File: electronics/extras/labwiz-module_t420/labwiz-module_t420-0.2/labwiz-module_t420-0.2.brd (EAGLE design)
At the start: 65.8 x 35.2 mm, 47 parts, among them IC1 MCP3424, U1 MCP9800

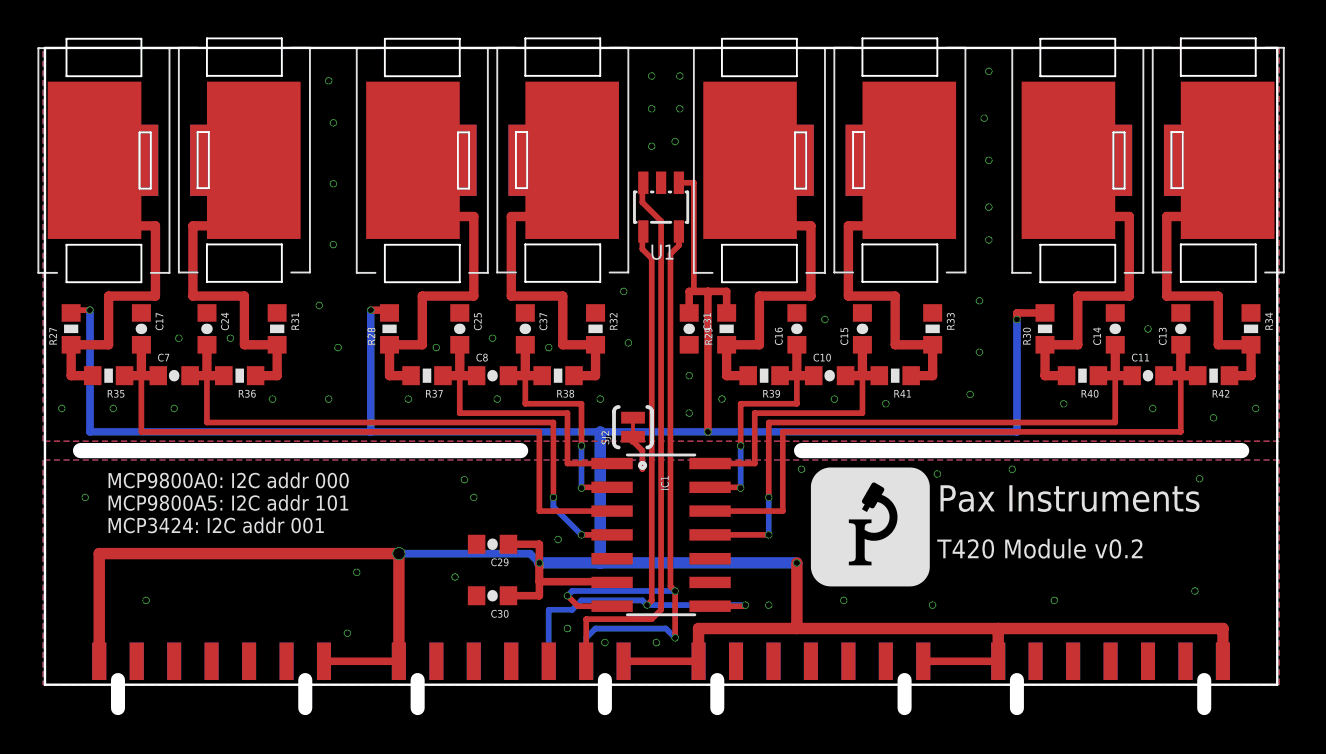
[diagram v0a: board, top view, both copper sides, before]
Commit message: Updated full-breakout and T420 modules. Boards ordered.
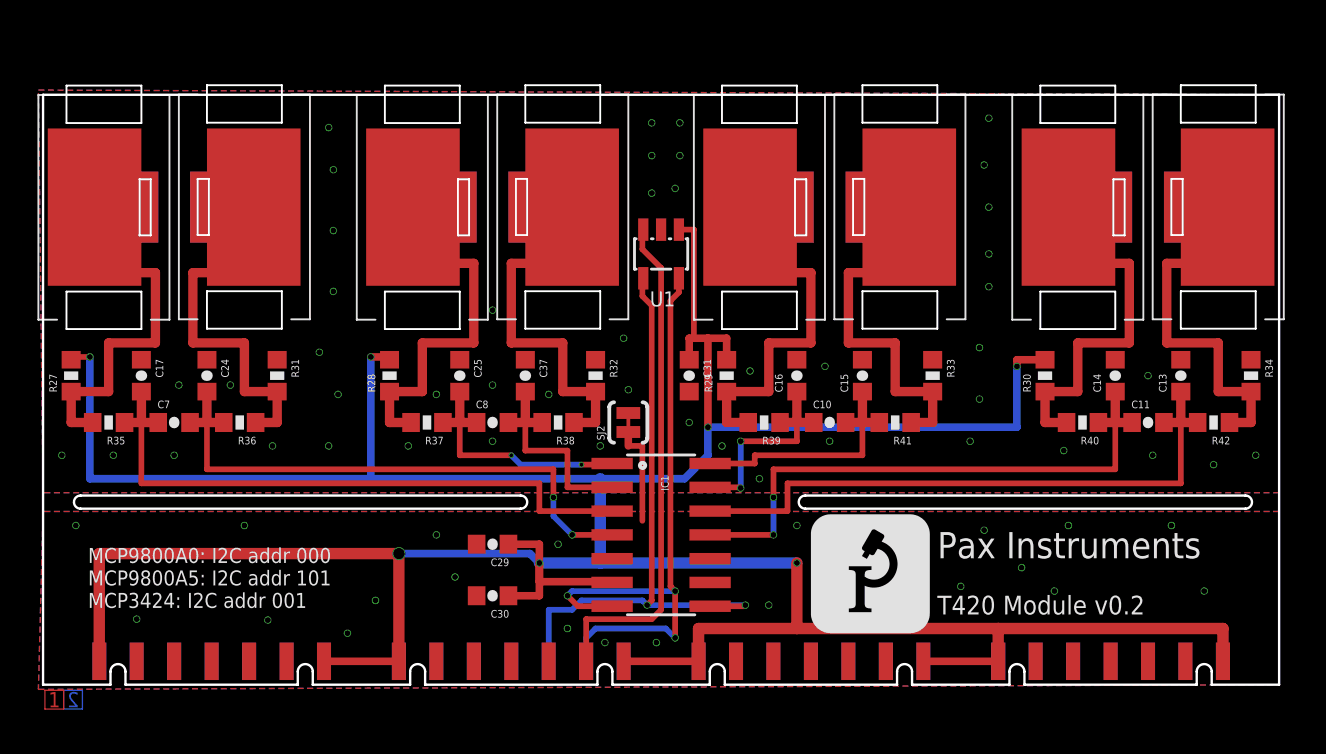
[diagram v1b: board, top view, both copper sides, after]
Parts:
- added U$2: (no value), PaxInstruments-Aesthetics:LAYERS-LABEL-2
- moved C10 2.50 mm to (42.0, 14.0)
- moved C11 2.50 mm to (59.0, 14.0)
- moved C13 2.50 mm to (60.8, 16.5)
- moved C14 2.50 mm to (57.2, 16.5)
- moved C15 2.50 mm to (43.8, 16.5)
- moved C16 2.50 mm to (40.2, 16.5)
- moved C17 2.50 mm to (5.25, 16.5)
- moved C24 2.50 mm to (8.75, 16.5)
- moved C25 2.50 mm to (22.2, 16.5)
- moved C31 2.50 mm to (34.5, 16.5)
- moved C37 2.50 mm to (25.8, 16.5)
- moved C7 2.50 mm to (7.00, 14.0)
- moved C8 2.50 mm to (24.0, 14.0)
- moved R27 2.50 mm to (1.50, 16.5)
- moved R28 2.50 mm to (18.5, 16.5)
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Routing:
- net 3.3V: track 207.2 -> 201.2 mm
- net GND: track 1.95 -> 5.49 mm, vias 20 -> 21
- net TC2+: track 16.3 -> 13.6 mm, vias 0 -> 2
- net TC2-: track 14.1 -> 11.5 mm, vias 2 -> 0
- net TC4-: track 35.8 -> 33.3 mm
- net TC4+: track 33.6 -> 31.1 mm
- net TC1+: track 35.8 -> 33.3 mm
- net I2C1_SCL: track 35.8 -> 33.3 mm
- net ALERT: track 29.7 -> 27.2 mm
- net TC3+: track 14.1 -> 11.6 mm
- net TC3-: track 16.3 -> 13.8 mm
- net I2C1_SDA: track 36.9 -> 34.4 mm
- net TC1-: track 32.7 -> 30.5 mm
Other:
- board size 65.8 x 35.2 mm -> 66 x 31.5 mm
- board text added: "Height restriction 4.7 mm"
